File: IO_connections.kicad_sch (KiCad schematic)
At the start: 8 parts, among them J1 LCD_Conn, J2 XT60 - M, J3 IMU_FFC_Conn, J4 JTAG_Conn, J5 IR_LED, J6 IR_SENSOR, J7 ESC_Conn

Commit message: Divided project
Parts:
- added 3V3, CS1, GND1, INT1, MISO1, MOSI1, SCK1: ~, TestPoint:TestPoint_Pad_D2.0mm, symbol Connector:TestPoint
- J2: footprint Connector_AMASS:AMASS_XT60PW-M_1x02_P7.20mm_Horizontal -> Library:XT60-SURF
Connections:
- net +3.3V: now also 3V3.1
- net GND: now also GND1.1
- net IMU_CS: now also CS1.1
- net IMU_INT: now also INT1.1
- net IMU_MISO: now also MISO1.1
- net IMU_MOSI: now also MOSI1.1
- net IMU_SCK: now also SCK1.1
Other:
- moved on the sheet: J3

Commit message: DPB mainboard_v1 completed
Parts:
- removed J4: JTAG_Conn, Connector_PinHeader_2.54mm:PinHeader_1x06_P2.54mm_Vertical, symbol Connector_Generic:Conn_01x06
- J5: renamed from J7; footprint (none) -> TerminalBlock:TerminalBlock_bornier-4_P5.08mm
- J7: renamed from J2; footprint Library:XT60-SURF -> Connector_AMASS:AMASS_XT60PW-M_1x02_P7.20mm_Horizontal; LCSC (none) -> C98732
- renumbered 3V3 to 3V1, J1 to J2
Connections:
- net LCD_T_CLK is gone; now on net LCD_SCK: J2.10 (Pin_10)
- net LCD_T_DIN is gone; now on net LCD_MOSI: J2.12 (Pin_12)
- net LCD_T_DOUT is gone; now on net LCD_MISO: J2.13 (Pin_13)
- net LCD_MISO: now reaches J2.9 (Pin_9)
- net JTAG_TCK: no longer names the net of D9.5 (K)
- net JTAG_TDI: no longer names the net of D9.4 (K)
- net JTAG_TDO: no longer names the net of D9.3 (K)
- net JTAG_TMS: no longer names the net of D9.6 (K)
- no-connect marks 2 -> 5
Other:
- note removed: "JTAG"
- moved on the sheet: J5, J7

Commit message: On production | V0.1
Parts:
- 3V1, CS1, GND1, INT1, J2, J5, J6, MISO1, MOSI1, SCK1: now left out of the parts list
- D9: footprint Package_TO_SOT_SMD:SOT-23-6 -> Package_TO_SOT_SMD:SOT-23-6_Handsoldering
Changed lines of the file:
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@@
       (effects (font (size 1.27 1.27)))
     )
-    (property "Footprint" "Package_TO_SOT_SMD:SOT-23-6" (at 44.45 130.81 0)
+    (property "Footprint" "Package_TO_SOT_SMD:SOT-23-6_Handsoldering" (at 44.45 130.81 0)
       (effects (font (size 1.27 1.27)) (justify left) hide)
     )
@@
   )
   (symbol (lib_id "Connector:TestPoint") (at 115.57 74.93 270) (unit 1)
-    (in_bom yes) (on_board yes) (dnp no) (fields_autoplaced)
+    (in_bom no) (on_board yes) (dnp no) (fields_autoplaced)
     (property "Reference" "MISO1" (at 120.65 74.295 90)
       (effects (font (size 1.27 1.27)) (justify left))
@@
   )
   (symbol (lib_id "Connector_Generic:Conn_01x04") (at 180.34 45.72 0) (unit 1)
-    (in_bom yes) (on_board yes) (dnp no) (fields_autoplaced)
+    (in_bom no) (on_board yes) (dnp no) (fields_autoplaced)
     (property "Reference" "J5" (at 182.88 46.355 0)
       (effects (font (size 1.27 1.27)) (justify left))
@@
   )
   (symbol (lib_id "Connector_Generic:Conn_01x02") (at 196.85 82.55 0) (unit 1)
-    (in_bom yes) (on_board yes) (dnp no) (fields_autoplaced)
+    (in_bom no) (on_board yes) (dnp no) (fields_autoplaced)
     (property "Reference" "J5" (at 199.39 83.185 0)
       (effects (font (size 1.27 1.27)) (justify left))
@@
   )
   (symbol (lib_id "Connector:TestPoint") (at 115.57 67.31 270) (unit 1)
-    (in_bom yes) (on_board yes) (dnp no) (fields_autoplaced)
+    (in_bom no) (on_board yes) (dnp no) (fields_autoplaced)
     (property "Reference" "3V1" (at 120.65 66.675 90)
       (effects (font (size 1.27 1.27)) (justify left))
@@
   )
   (symbol (lib_id "Connector:TestPoint") (at 115.57 80.01 270) (unit 1)
-    (in_bom yes) (on_board yes) (dnp no) (fields_autoplaced)
+    (in_bom no) (on_board yes) (dnp no) (fields_autoplaced)
     (property "Reference" "CS1" (at 120.65 79.375 90)
       (effects (font (size 1.27 1.27)) (justify left))
@@
   )
   (symbol (lib_id "Connector_Generic:Conn_01x14") (at 57.15 60.96 0) (unit 1)
-    (in_bom yes) (on_board yes) (dnp no) (fields_autoplaced)
+    (in_bom no) (on_board yes) (dnp no) (fields_autoplaced)
     (property "Reference" "J2" (at 59.69 61.595 0)
       (effects (font (size 1.27 1.27)) (justify left))
@@
   )
   (symbol (lib_id "Connector:TestPoint") (at 115.57 82.55 270) (unit 1)
-    (in_bom yes) (on_board yes) (dnp no) (fields_autoplaced)
+    (in_bom no) (on_board yes) (dnp no) (fields_autoplaced)
     (property "Reference" "INT1" (at 120.65 81.915 90)
       (effects (font (size 1.27 1.27)) (justify left))
@@
   )
   (symbol (lib_id "Connector:TestPoint") (at 115.57 69.85 270) (unit 1)
-    (in_bom yes) (on_board yes) (dnp no) (fields_autoplaced)
+    (in_bom no) (on_board yes) (dnp no) (fields_autoplaced)
     (property "Reference" "GND1" (at 120.65 69.215 90)
       (effects (font (size 1.27 1.27)) (justify left))
@@
   )
   (symbol (lib_id "Connector_Generic:Conn_01x02") (at 162.56 82.55 0) (unit 1)
-    (in_bom yes) (on_board yes) (dnp no) (fields_autoplaced)
+    (in_bom no) (on_board yes) (dnp no) (fields_autoplaced)
     (property "Reference" "J6" (at 165.1 83.185 0)
       (effects (font (size 1.27 1.27)) (justify left))
@@
   )
   (symbol (lib_id "Connector:TestPoint") (at 115.57 77.47 270) (unit 1)
-    (in_bom yes) (on_board yes) (dnp no) (fields_autoplaced)
+    (in_bom no) (on_board yes) (dnp no) (fields_autoplaced)
     (property "Reference" "SCK1" (at 120.65 76.835 90)
       (effects (font (size 1.27 1.27)) (justify left))
@@
   )
   (symbol (lib_id "Connector:TestPoint") (at 115.57 72.39 270) (unit 1)
-    (in_bom yes) (on_board yes) (dnp no) (fields_autoplaced)
+    (in_bom no) (on_board yes) (dnp no) (fields_autoplaced)
     (property "Reference" "MOSI1" (at 120.65 71.755 90)
       (effects (font (size 1.27 1.27)) (justify left))

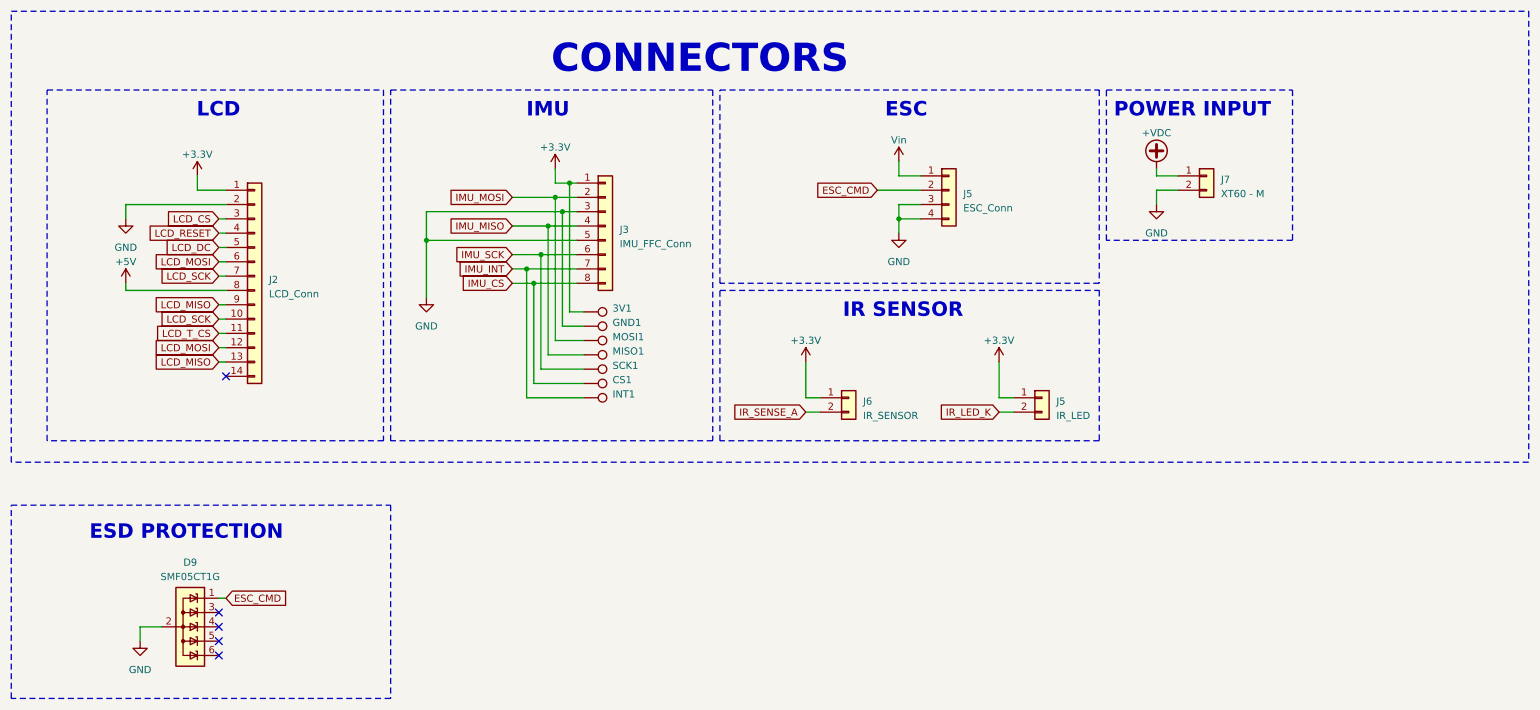
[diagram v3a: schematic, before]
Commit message: Add hysteresis to IR sensor. Update README file.
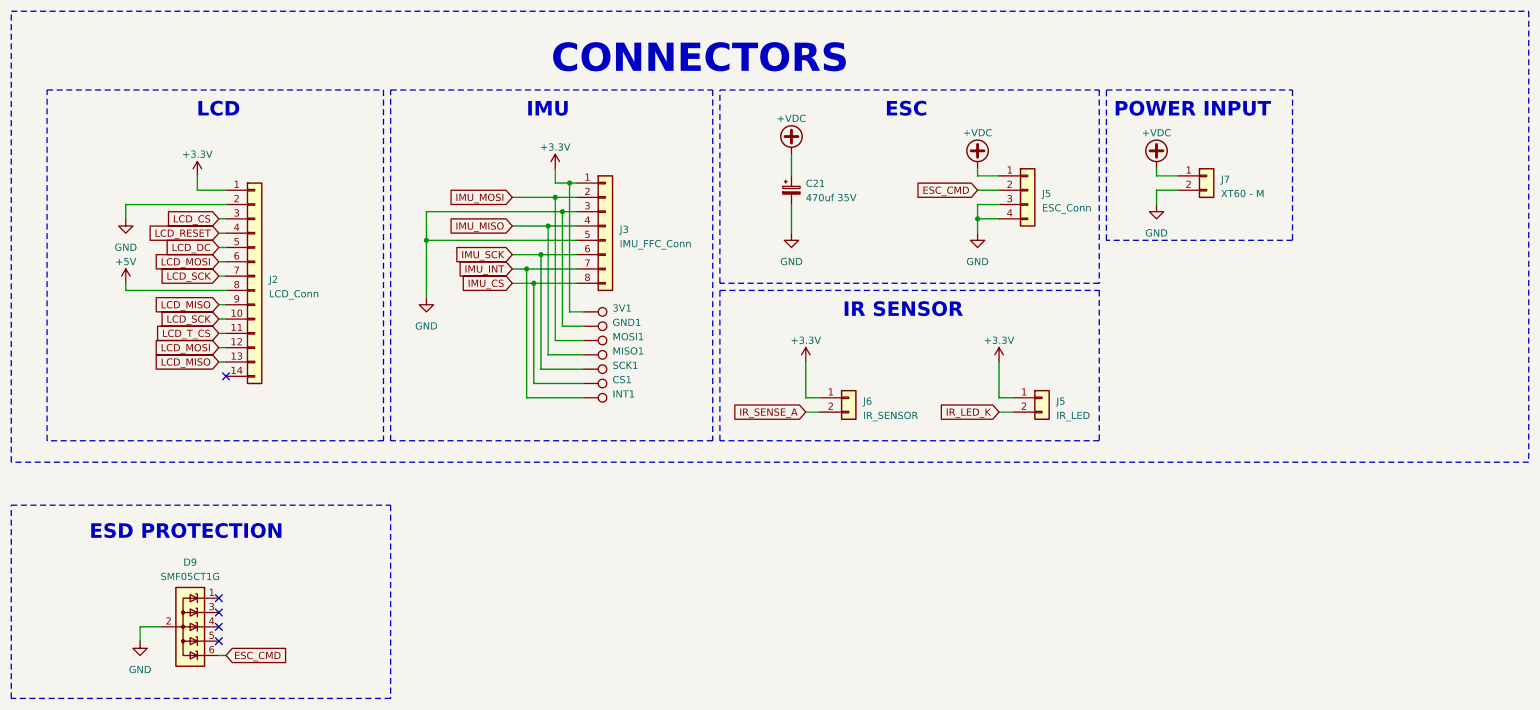
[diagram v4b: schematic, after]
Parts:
- added C21: 470uf 35V, Capacitor_SMD:CP_Elec_10x14.3, symbol Device:C_Polarized_Small
- D9: footprint Package_TO_SOT_SMD:SOT-23-6_Handsoldering -> Package_TO_SOT_SMD:SOT-363_SC-70-6
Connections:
- net VCC is gone; now on net +VDC: J5.1 (Pin_1)
- net +VDC: now also C21.1
- net ESC_CMD: now also D9.6 (K); no longer D9.1 (K)
- net GND: now also C21.2
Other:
- moved on the sheet: J5
